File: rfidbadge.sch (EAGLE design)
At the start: 25 parts, among them Q1 BSS123, U1 ATMEGA328P_TQFP, U2 CLRC663, Y1 27.12 MHz

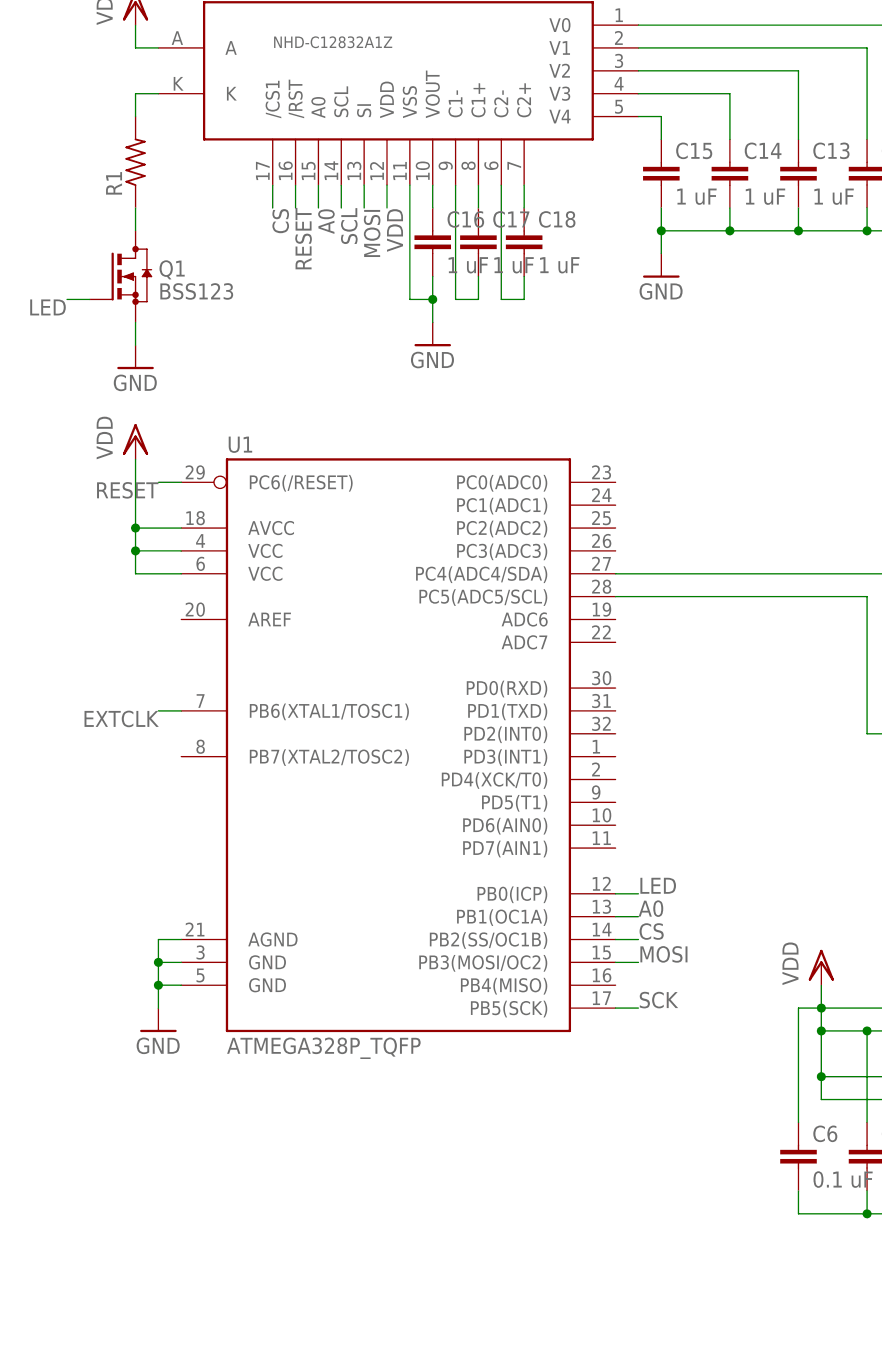
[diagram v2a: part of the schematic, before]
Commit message: Add ISP and FTDI headers
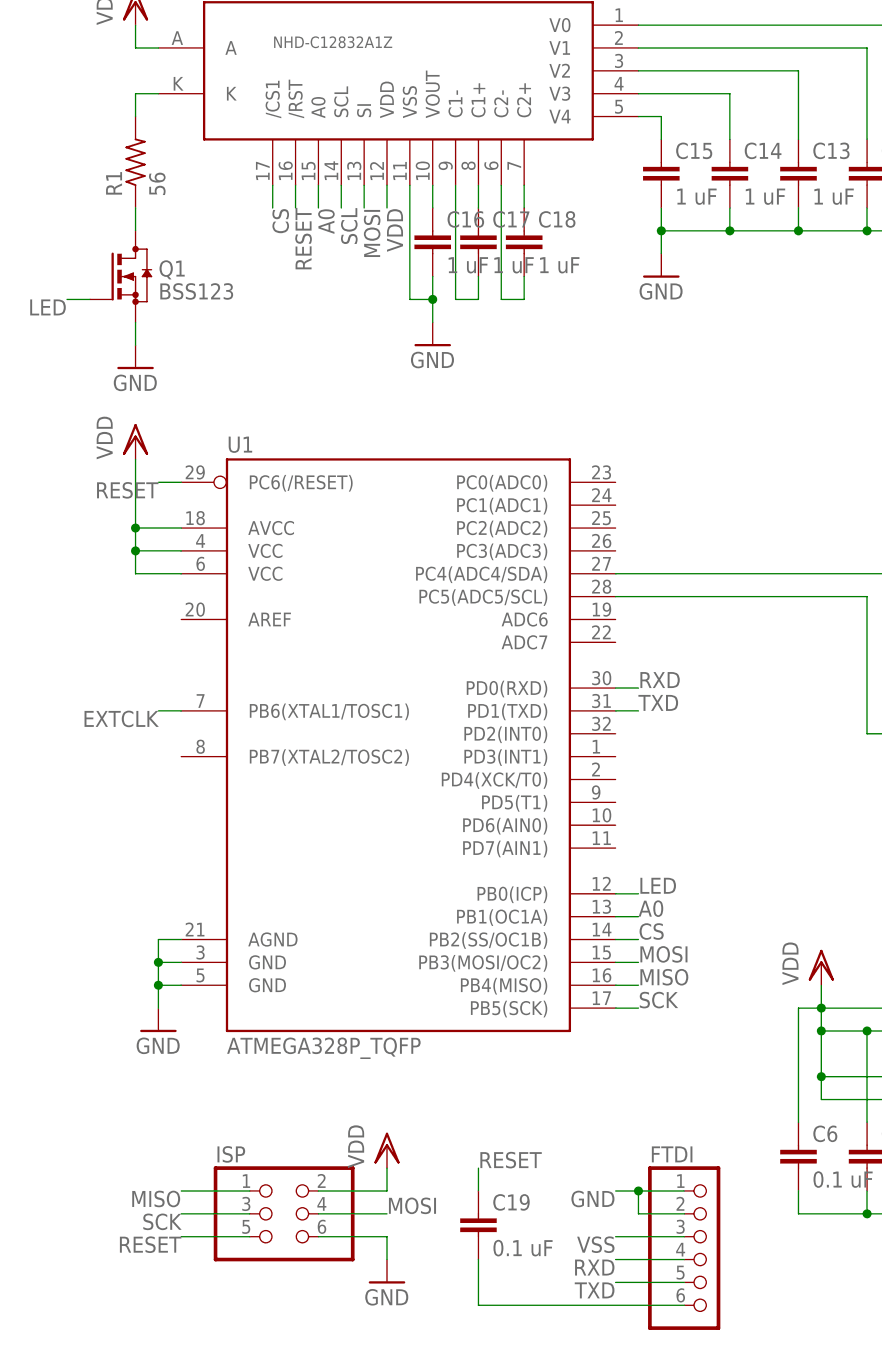
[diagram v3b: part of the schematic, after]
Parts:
- added C19: 0.1 uF, rcl:C-EUC0603K
- added FTDI: (no value), pinhead:PINHD-1X6
- added ISP: (no value), pinhead:PINHD-2X3
- R1: value (none) -> 56
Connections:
- new net MISO: ISP.1, U1.PB4(MISO)
- new net N$19: C19.2, FTDI.6
- new net RXD: FTDI.4, U1.PD0(RXD)
- new net TXD: FTDI.5, U1.PD1(TXD)
- net GND: now also FTDI.1, FTDI.2, ISP.6
- net MOSI: now also ISP.4
- net RESET: now also C19.1, ISP.5
- net SCK: now also ISP.3
- net VDD: now also ISP.2
- net VSS: now also FTDI.3
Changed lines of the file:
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@@
 <part name="GND7" library="supply1" deviceset="GND" device=""/>
 <part name="VDD4" library="supply1" deviceset="VDD" device=""/>
-<part name="R1" library="rcl" deviceset="R-US_" device="R0603"/>
+<part name="R1" library="rcl" deviceset="R-US_" device="R0603" value="56"/>
 <part name="Q1" library="transistor-small-signal" deviceset="BSS123" device=""/>
 <part name="GND8" library="supply1" deviceset="GND" device=""/>
+<part name="ISP" library="pinhead" deviceset="PINHD-2X3" device=""/>
+<part name="VDD5" library="supply1" deviceset="VDD" device=""/>
+<part name="GND9" library="supply1" deviceset="GND" device=""/>
+<part name="FTDI" library="pinhead" deviceset="PINHD-1X6" device=""/>
+<part name="C19" library="rcl" deviceset="C-EU" device="C0603K" value="0.1 uF">
+<attribute name="PROD_ID" value="311-1088-1-ND"/>
+</part>
 </parts>
 <sheets>
@@
 <instance part="Q1" gate="G$1" x="-30.48" y="53.34"/>
 <instance part="GND8" gate="1" x="-30.48" y="43.18"/>
+<instance part="ISP" gate="A" x="-15.24" y="-50.8"/>
+<instance part="VDD5" gate="G$1" x="-2.54" y="-43.18"/>
+<instance part="GND9" gate="1" x="-2.54" y="-58.42"/>
+<instance part="FTDI" gate="A" x="33.02" y="-55.88"/>
+<instance part="C19" gate="G$1" x="7.62" y="-50.8">
+<attribute name="PROD_ID" x="7.62" y="-50.8" size="1.778" layer="96" display="off"/>
+</instance>
 </instances>
 <busses>
@@
 <pinref part="GND8" gate="1" pin="GND"/>
 <wire x1="-30.48" y1="48.26" x2="-30.48" y2="45.72" width="0.1524" layer="91"/>
+</segment>
+<segment>
+<pinref part="ISP" gate="A" pin="6"/>
+<pinref part="GND9" gate="1" pin="GND"/>
+<wire x1="-10.16" y1="-53.34" x2="-2.54" y2="-53.34" width="0.1524" layer="91"/>
+<wire x1="-2.54" y1="-53.34" x2="-2.54" y2="-55.88" width="0.1524" layer="91"/>
+</segment>
+<segment>
+<pinref part="FTDI" gate="A" pin="1"/>
+<wire x1="30.48" y1="-48.26" x2="25.4" y2="-48.26" width="0.1524" layer="91"/>
+<label x="22.86" y="-48.26" size="1.778" layer="95" rot="R180"/>
+<pinref part="FTDI" gate="A" pin="2"/>
+<wire x1="25.4" y1="-48.26" x2="22.86" y2="-48.26" width="0.1524" layer="91"/>
+<wire x1="30.48" y1="-50.8" x2="25.4" y2="-50.8" width="0.1524" layer="91"/>
+<wire x1="25.4" y1="-50.8" x2="25.4" y2="-48.26" width="0.1524" layer="91"/>
+<junction x="25.4" y="-48.26"/>
 </segment>
 </net>
@@
 <wire x1="-30.48" y1="78.74" x2="-30.48" y2="81.28" width="0.1524" layer="91"/>
 </segment>
+<segment>
+<pinref part="ISP" gate="A" pin="2"/>
+<pinref part="VDD5" gate="G$1" pin="VDD"/>
+<wire x1="-10.16" y1="-48.26" x2="-2.54" y2="-48.26" width="0.1524" layer="91"/>
+<wire x1="-2.54" y1="-48.26" x2="-2.54" y2="-45.72" width="0.1524" layer="91"/>
+</segment>
 </net>
 <net name="N$8" class="0">
@@
 <label x="66.04" y="7.62" size="1.778" layer="95" rot="R180"/>
 </segment>
+<segment>
+<pinref part="FTDI" gate="A" pin="3"/>
+<wire x1="30.48" y1="-53.34" x2="22.86" y2="-53.34" width="0.1524" layer="91"/>
+<label x="22.86" y="-53.34" size="1.778" layer="95" rot="R180"/>
+</segment>
 </net>
 <net name="N$3" class="0">
@@
 <label x="25.4" y="-22.86" size="1.778" layer="95"/>
 </segment>
+<segment>
+<pinref part="ISP" gate="A" pin="4"/>
+<wire x1="-10.16" y1="-50.8" x2="-2.54" y2="-50.8" width="0.1524" layer="91"/>
+<label x="-2.54" y="-50.8" size="1.778" layer="95"/>
+</segment>
 </net>
 <net name="SCL" class="0">
@@
 <label x="25.4" y="-27.94" size="1.778" layer="95"/>
 </segment>
+<segment>
+<pinref part="ISP" gate="A" pin="3"/>
+<wire x1="-17.78" y1="-50.8" x2="-25.4" y2="-50.8" width="0.1524" layer="91"/>
+<label x="-25.4" y="-50.8" size="1.778" layer="95" rot="R180"/>
+</segment>
 </net>
 <net name="A0" class="0">
@@
 <wire x1="-25.4" y1="30.48" x2="-27.94" y2="30.48" width="0.1524" layer="91"/>
 <label x="-27.94" y="30.48" size="1.778" layer="95" rot="R180"/>
+</segment>
+<segment>
+<pinref part="ISP" gate="A" pin="5"/>
+<wire x1="-17.78" y1="-53.34" x2="-25.4" y2="-53.34" width="0.1524" layer="91"/>
+<label x="-25.4" y="-53.34" size="1.778" layer="95" rot="R180"/>
+</segment>
+<segment>
+<pinref part="C19" gate="G$1" pin="1"/>
+<wire x1="7.62" y1="-48.26" x2="7.62" y2="-45.72" width="0.1524" layer="91"/>
+<label x="7.62" y="-45.72" size="1.778" layer="95"/>
 </segment>
 </net>
@@
 </segment>
 </net>
+<net name="MISO" class="0">
+<segment>
+<pinref part="ISP" gate="A" pin="1"/>
+<wire x1="-17.78" y1="-48.26" x2="-25.4" y2="-48.26" width="0.1524" layer="91"/>
+<label x="-25.4" y="-48.26" size="1.778" layer="95" rot="R180"/>
+</segment>
+<segment>
+<pinref part="U1" gate="U$1" pin="PB4(MISO)"/>
+<wire x1="22.86" y1="-25.4" x2="25.4" y2="-25.4" width="0.1524" layer="91"/>
+<label x="25.4" y="-25.4" size="1.778" layer="95"/>
+</segment>
+</net>
+<net name="TXD" class="0">
+<segment>
+<pinref part="U1" gate="U$1" pin="PD1(TXD)"/>
+<wire x1="22.86" y1="5.08" x2="25.4" y2="5.08" width="0.1524" layer="91"/>
+<label x="25.4" y="5.08" size="1.778" layer="95"/>
+</segment>
+<segment>
+<pinref part="FTDI" gate="A" pin="5"/>
+<wire x1="30.48" y1="-58.42" x2="22.86" y2="-58.42" width="0.1524" layer="91"/>
+<label x="22.86" y="-58.42" size="1.778" layer="95" rot="R180"/>
+</segment>
+</net>
+<net name="RXD" class="0">
+<segment>
+<pinref part="U1" gate="U$1" pin="PD0(RXD)"/>
+<wire x1="22.86" y1="7.62" x2="25.4" y2="7.62" width="0.1524" layer="91"/>
+<label x="25.4" y="7.62" size="1.778" layer="95"/>
+</segment>
+<segment>
+<pinref part="FTDI" gate="A" pin="4"/>
+<wire x1="30.48" y1="-55.88" x2="22.86" y2="-55.88" width="0.1524" layer="91"/>
+<label x="22.86" y="-55.88" size="1.778" layer="95" rot="R180"/>
+</segment>
+</net>
+<net name="N$19" class="0">
+<segment>
+<pinref part="FTDI" gate="A" pin="6"/>
+<wire x1="30.48" y1="-60.96" x2="7.62" y2="-60.96" width="0.1524" layer="91"/>
+<pinref part="C19" gate="G$1" pin="2"/>
+<wire x1="7.62" y1="-60.96" x2="7.62" y2="-55.88" width="0.1524" layer="91"/>
+</segment>
+</net>

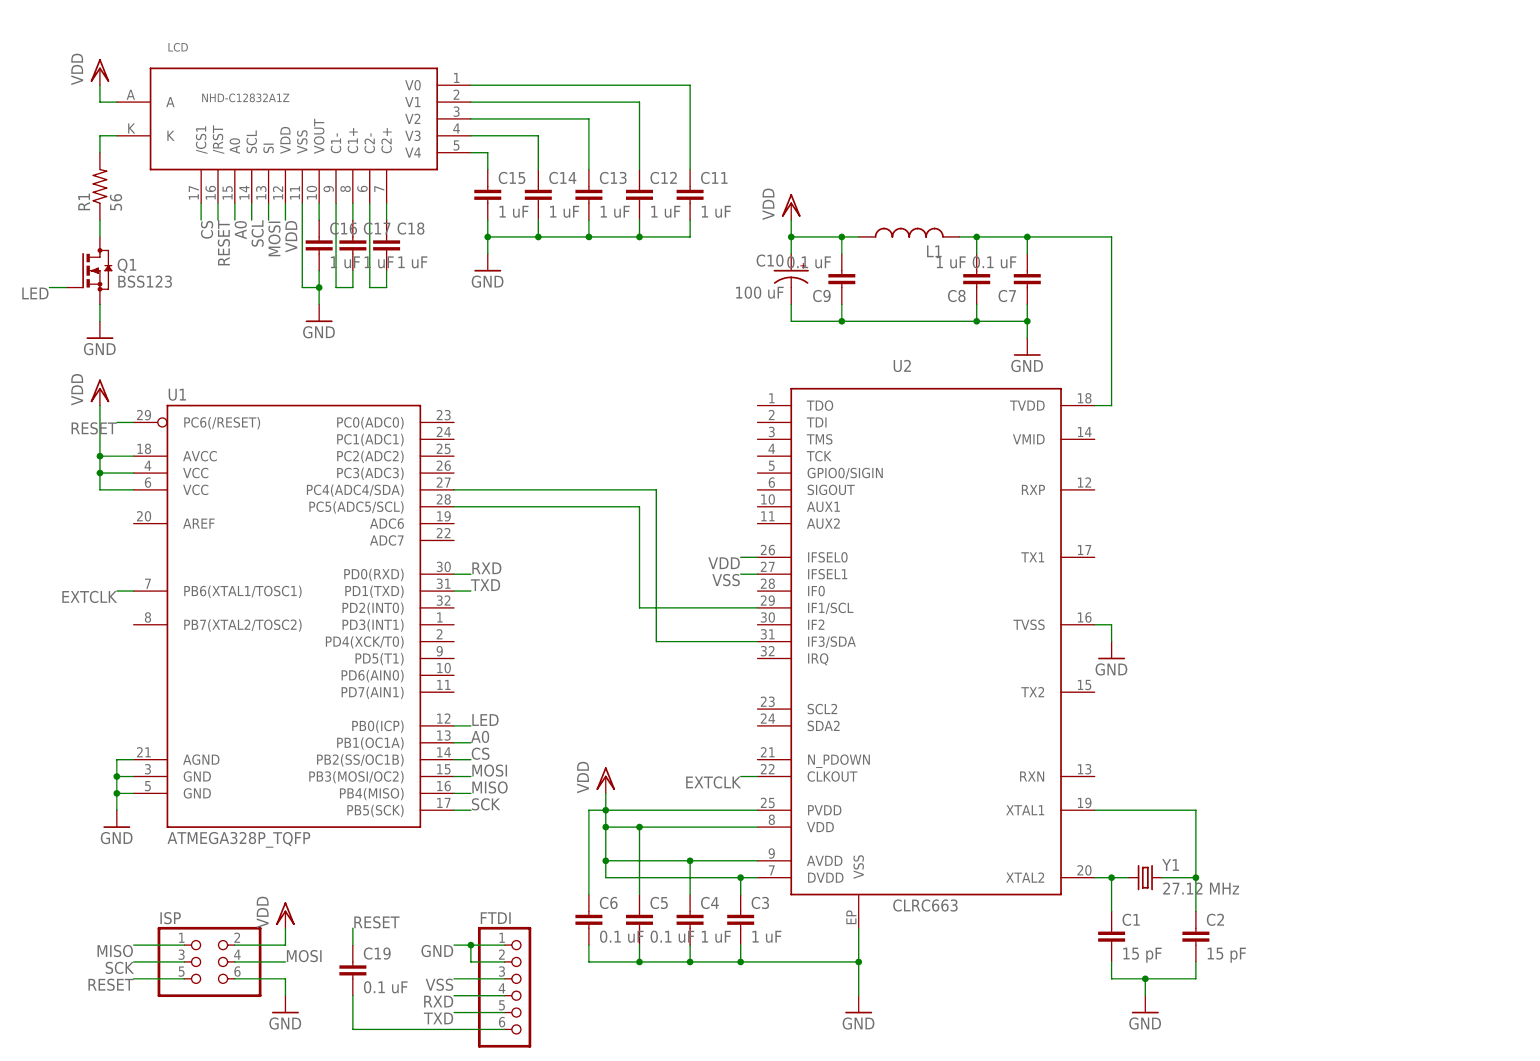
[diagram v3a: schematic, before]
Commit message: Add antenna circuit
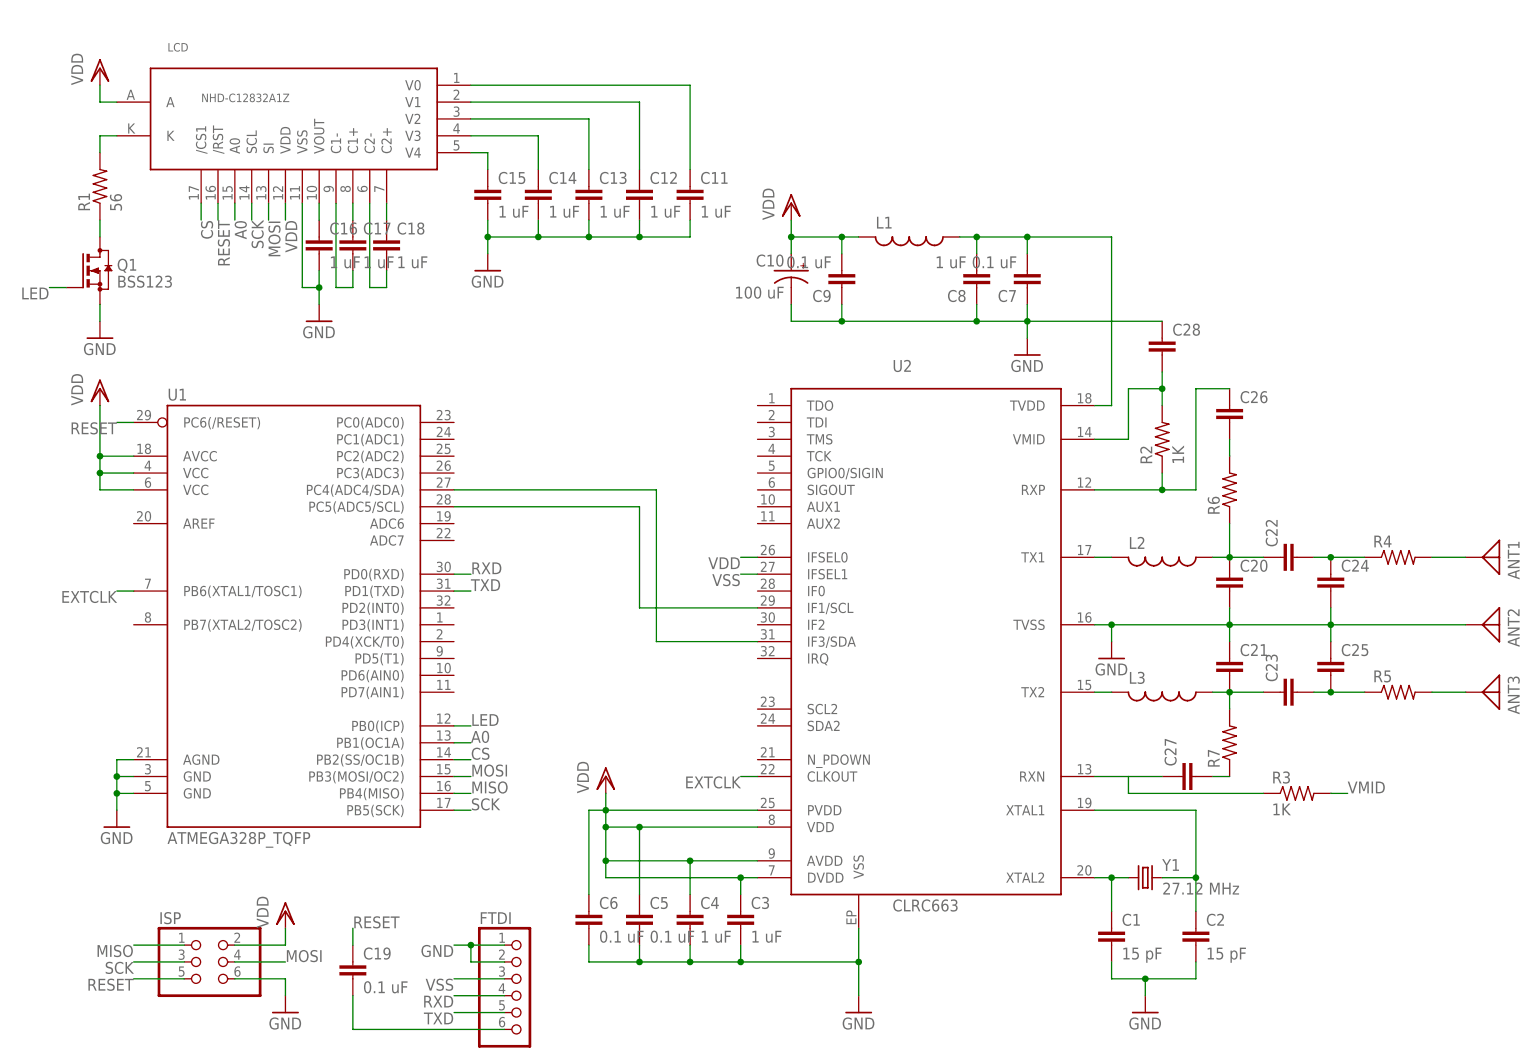
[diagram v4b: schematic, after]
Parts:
- added ANT1, ANT2, ANT3: (no value), discrete:ANTENNA
- added C20, C21, C22, C23, C24, C25, C26, C27, C28: (no value), rcl:C-EUC0603K
- added L2, L3: (no value), rcl:L-USL0201
- added R2, R3: 1K, rcl:R-US_R0603
- added R4, R5, R6, R7: (no value), rcl:R-US_R0603
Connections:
- net N$1 renamed XTAL2
- net N$10 renamed V0
- net N$11 renamed C2+
- net N$12 renamed C2-
- net N$13 renamed C1+
- net N$14 renamed C1-
- net N$15 renamed VOUT
- net N$16 renamed K
- net N$2 renamed XTAL1
- net N$3 renamed V4
- net N$4 renamed SDA
- net N$6 renamed V3
- net N$7 renamed V2
- net N$9 renamed V1
- new net N$1: C20.1, C22.1, L2.1, R6.1
- new net N$2: C21.2, C23.1, L3.1, R7.2
- new net N$3: C22.2, C24.1, R4.1
- new net N$4: C23.2, C25.2, R5.1
- new net N$6: ANT3.1, R5.2
- new net N$7: C26.2, R6.2
- new net N$9: C27.1, R3.1, U2.RXN
- new net RXP: C26.1, R2.1, U2.RXP
- new net TVDD: C7.2, C8.2, L1.1, U2.TVDD
- new net TX1: L2.2, U2.TX1
- new net TX2: L3.2, U2.TX2
- new net VMID: C28.2, R2.2, R3.2, U2.VMID
- net GND: now also ANT2.1, C20.2, C21.1, C24.2, C25.1, C28.1
- net N$5: now also ANT1.1, R4.2; no longer U1.PC5(ADC5/SCL), U2.IF1/SCL
- net N$8: now also C27.2, R7.1; no longer C7.2, C8.2, L1.2, U2.TVDD
- net SCK: now also LCD.SCL
- net SCL: now also U1.PC5(ADC5/SCL), U2.IF1/SCL; no longer LCD.SCL
- net VDD: now also L1.2; no longer L1.1
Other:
- moved on the sheet: L1

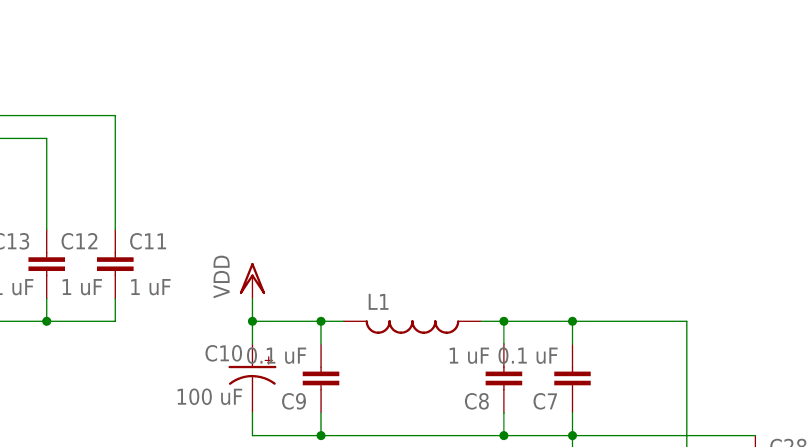
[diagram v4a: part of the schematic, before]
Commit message: Add AAAx3 battery holder
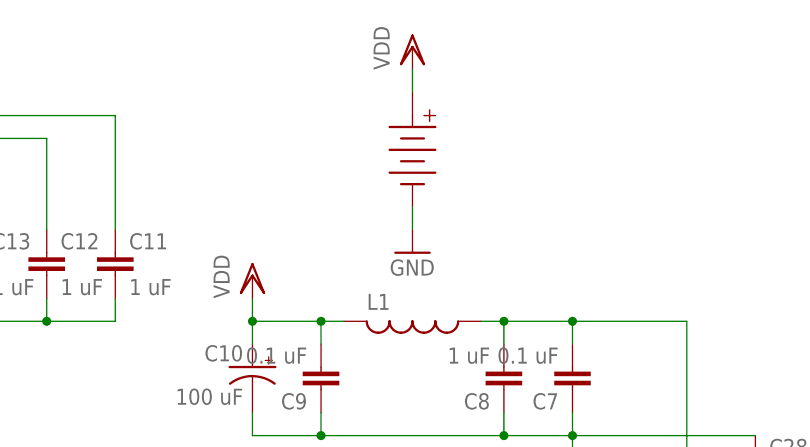
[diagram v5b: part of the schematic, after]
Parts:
- added U$1: AAA_X3, battery_holder:AAA_X3
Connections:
- net GND: now also U$1.P$1
- net VDD: now also U$1.P$2
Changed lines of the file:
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@@
 <attribute name="PROD_ID" value="311-1060-1-ND"/>
 </part>
+<part name="U$1" library="battery_holder" deviceset="AAA_X3" device=""/>
+<part name="GND10" library="supply1" deviceset="GND" device=""/>
+<part name="VDD6" library="supply1" deviceset="VDD" device=""/>
 </parts>
 <sheets>
@@
 <attribute name="PROD_ID" x="129.54" y="43.18" size="1.778" layer="96" display="off"/>
 </instance>
+<instance part="U$1" gate="G$1" x="91.44" y="76.2"/>
+<instance part="GND10" gate="1" x="91.44" y="66.04"/>
+<instance part="VDD6" gate="G$1" x="91.44" y="88.9"/>
 </instances>
 <busses>
@@
 <wire x1="25.4" y1="-50.8" x2="25.4" y2="-48.26" width="0.1524" layer="91"/>
 <junction x="25.4" y="-48.26"/>
+</segment>
+<segment>
+<pinref part="U$1" gate="G$1" pin="P$1"/>
+<pinref part="GND10" gate="1" pin="GND"/>
+<wire x1="91.44" y1="71.12" x2="91.44" y2="68.58" width="0.1524" layer="91"/>
 </segment>
 </net>
@@
 <wire x1="-2.54" y1="-48.26" x2="-2.54" y2="-45.72" width="0.1524" layer="91"/>
 </segment>
+<segment>
+<pinref part="VDD6" gate="G$1" pin="VDD"/>
+<pinref part="U$1" gate="G$1" pin="P$2"/>
+<wire x1="91.44" y1="86.36" x2="91.44" y2="83.82" width="0.1524" layer="91"/>
+</segment>
 </net>
